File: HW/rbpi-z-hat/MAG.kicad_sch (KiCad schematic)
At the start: 0 parts

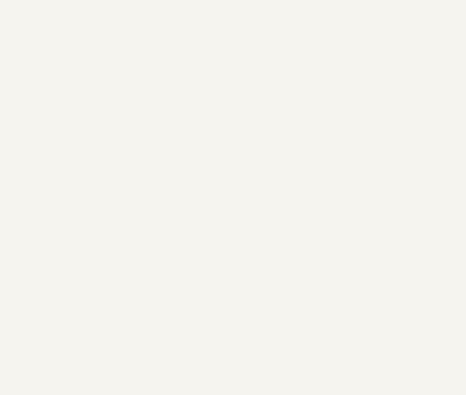
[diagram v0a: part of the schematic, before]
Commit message: Added schematics for QMC5883L
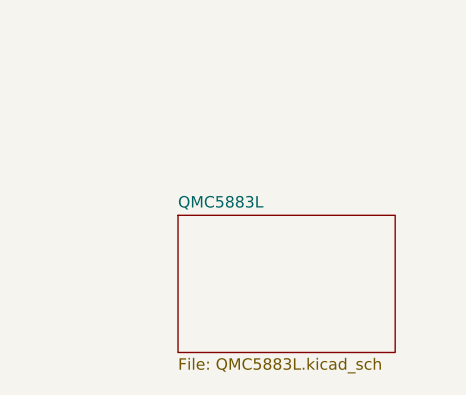
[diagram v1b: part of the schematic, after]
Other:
- added sheet QMC5883L (QMC5883L.kicad_sch)
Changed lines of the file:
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@@
     (stroke (width 0) (type default))
+  )
+  (sheet (at 85.09 142.24) (size 24.13 15.24) (fields_autoplaced)
+    (stroke (width 0.1524) (type solid))
+    (fill (color 0 0 0 0.0000))
+    (property "Sheetname" "QMC5883L" (at 85.09 141.5284 0)
+      (effects (font (size 1.27 1.27)) (justify left bottom))
+    )
+    (property "Sheetfile" "QMC5883L.kicad_sch" (at 85.09 158.0646 0)
+      (effects (font (size 1.27 1.27)) (justify left top))
+    )
+    (instances
+      (project "rbpi-z-hat"
+        (path "/d99b0340-d795-4b40-9cde-9851c6cee99d/740a9ed9-3c23-4e4f-8dd1-04f07ce4215e" (page "19"))
+      )
+    )
   )
   (sheet (at 82.55 74.93) (size 24.13 21.59) (fields_autoplaced)

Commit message: Apdated Sch and PCB
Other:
- sheet QMC5883L ports: added QMC_GND, QMC_INT, QMC_SCL, QMC_SDA, QMC_VDD; removed none
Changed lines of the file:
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@@
     (comment 2 "Denis Tsekh")
   )
-  (wire (pts (xy 67.31 93.98) (xy 82.55 93.98))
+  (junction (at 95.25 139.7) (diameter 0) (color 0 0 0 0)
+  )
+  (junction (at 104.14 128.27) (diameter 0) (color 0 0 0 0)
+  )
+  (junction (at 97.79 142.24) (diameter 0) (color 0 0 0 0)
+  )
+  (junction (at 101.6 125.73) (diameter 0) (color 0 0 0 0)
+  )
+  (wire (pts (xy 91.44 142.24) (xy 97.79 142.24))
     (stroke (width 0) (type default))
   )
-  (wire (pts (xy 67.31 77.47) (xy 82.55 77.47))
+  (wire (pts (xy 91.44 125.73) (xy 101.6 125.73))
     (stroke (width 0) (type default))
   )
-  (wire (pts (xy 67.31 83.82) (xy 82.55 83.82))
+  (wire (pts (xy 104.14 128.27) (xy 106.68 128.27))
     (stroke (width 0) (type default))
   )
-  (wire (pts (xy 67.31 80.01) (xy 82.55 80.01))
+  (wire (pts (xy 91.44 132.08) (xy 106.68 132.08))
     (stroke (width 0) (type default))
   )
-  (wire (pts (xy 67.31 86.36) (xy 82.55 86.36))
+  (wire (pts (xy 104.14 128.27) (xy 104.14 161.29))
     (stroke (width 0) (type default))
   )
-  (wire (pts (xy 67.31 91.44) (xy 82.55 91.44))
+  (wire (pts (xy 91.44 128.27) (xy 104.14 128.27))
     (stroke (width 0) (type default))
   )
-  (sheet (at 85.09 142.24) (size 24.13 15.24) (fields_autoplaced)
+  (wire (pts (xy 104.14 161.29) (xy 106.68 161.29))
+    (stroke (width 0) (type default))
+  )
+  (wire (pts (xy 95.25 139.7) (xy 95.25 167.64))
+    (stroke (width 0) (type default))
+  )
+  (wire (pts (xy 97.79 170.18) (xy 106.68 170.18))
+    (stroke (width 0) (type default))
+  )
+  (wire (pts (xy 101.6 158.75) (xy 106.68 158.75))
+    (stroke (width 0) (type default))
+  )
+  (wire (pts (xy 95.25 139.7) (xy 106.68 139.7))
+    (stroke (width 0) (type default))
+  )
+  (wire (pts (xy 91.44 134.62) (xy 106.68 134.62))
+    (stroke (width 0) (type default))
+  )
+  (wire (pts (xy 91.44 163.83) (xy 106.68 163.83))
+    (stroke (width 0) (type default))
+  )
+  (wire (pts (xy 97.79 142.24) (xy 106.68 142.24))
+    (stroke (width 0) (type default))
+  )
+  (wire (pts (xy 95.25 167.64) (xy 106.68 167.64))
+    (stroke (width 0) (type default))
+  )
+  (wire (pts (xy 91.44 139.7) (xy 95.25 139.7))
+    (stroke (width 0) (type default))
+  )
+  (wire (pts (xy 101.6 125.73) (xy 101.6 158.75))
+    (stroke (width 0) (type default))
+  )
+  (wire (pts (xy 97.79 142.24) (xy 97.79 170.18))
+    (stroke (width 0) (type default))
+  )
+  (wire (pts (xy 101.6 125.73) (xy 106.68 125.73))
+    (stroke (width 0) (type default))
+  )
+  (hierarchical_label "MAG_SDA" (shape bidirectional) (at 91.44 125.73 180) (fields_autoplaced)
+    (effects (font (size 1.27 1.27)) (justify right))
+  )
+  (hierarchical_label "MAG_SCL" (shape input) (at 91.44 128.27 180) (fields_autoplaced)
+    (effects (font (size 1.27 1.27)) (justify right))
+  )
+  (hierarchical_label "MAG_GND" (shape input) (at 91.44 142.24 180) (fields_autoplaced)
+    (effects (font (size 1.27 1.27)) (justify right))
+  )
+  (hierarchical_label "MAG_IST_nRST" (shape input) (at 91.44 132.08 180) (fields_autoplaced)
+    (effects (font (size 1.27 1.27)) (justify right))
+  )
+  (hierarchical_label "MAG_VDD" (shape input) (at 91.44 139.7 180) (fields_autoplaced)
+    (effects (font (size 1.27 1.27)) (justify right))
+  )
+  (hierarchical_label "MAG_QMC_INT" (shape output) (at 91.44 163.83 180) (fields_autoplaced)
+    (effects (font (size 1.27 1.27)) (justify right))
+  )
+  (hierarchical_label "MAG_IST_DRDY" (shape output) (at 91.44 134.62 180) (fields_autoplaced)
+    (effects (font (size 1.27 1.27)) (justify right))
+  )
+  (sheet (at 106.68 156.21) (size 26.67 16.51) (fields_autoplaced)
     (stroke (width 0.1524) (type solid))
     (fill (color 0 0 0 0.0000))
-    (property "Sheetname" "QMC5883L" (at 85.09 141.5284 0)
+    (property "Sheetname" "QMC5883L" (at 106.68 155.4984 0)
       (effects (font (size 1.27 1.27)) (justify left bottom))
     )
-    (property "Sheetfile" "QMC5883L.kicad_sch" (at 85.09 158.0646 0)
+    (property "Sheetfile" "QMC5883L.kicad_sch" (at 106.68 173.3046 0)
       (effects (font (size 1.27 1.27)) (justify left top))
+    )
+    (pin "QMC_VDD" input (at 106.68 167.64 180)
+      (effects (font (size 1.27 1.27)) (justify left))
+    )
+    (pin "QMC_SCL" input (at 106.68 161.29 180)
+      (effects (font (size 1.27 1.27)) (justify left))
+    )
+    (pin "QMC_SDA" bidirectional (at 106.68 158.75 180)
+      (effects (font (size 1.27 1.27)) (justify left))
+    )
+    (pin "QMC_GND" input (at 106.68 170.18 180)
+      (effects (font (size 1.27 1.27)) (justify left))
+    )
+    (pin "QMC_INT" output (at 106.68 163.83 180)
+      (effects (font (size 1.27 1.27)) (justify left))
     )
     (instances
@@
     )
   )
-  (sheet (at 82.55 74.93) (size 24.13 21.59) (fields_autoplaced)
+  (sheet (at 106.68 123.19) (size 24.13 21.59) (fields_autoplaced)
     (stroke (width 0.1524) (type solid))
     (fill (color 0 0 0 0.0000))
-    (property "Sheetname" "IST8310" (at 82.55 74.2184 0)
+    (property "Sheetname" "IST8310" (at 106.68 122.4784 0)
       (effects (font (size 1.27 1.27)) (justify left bottom))
     )
-    (property "Sheetfile" "IST8310.kicad_sch" (at 82.55 97.1046 0)
+    (property "Sheetfile" "IST8310.kicad_sch" (at 106.68 145.3646 0)
       (effects (font (size 1.27 1.27)) (justify left top))
     )
-    (pin "IST_GND" input (at 82.55 93.98 180)
+    (pin "IST_GND" input (at 106.68 142.24 180)
       (effects (font (size 1.27 1.27)) (justify left))
     )
-    (pin "IST_VDD" input (at 82.55 91.44 180)
+    (pin "IST_VDD" input (at 106.68 139.7 180)
       (effects (font (size 1.27 1.27)) (justify left))
     )
-    (pin "IST_SDA" bidirectional (at 82.55 77.47 180)
+    (pin "IST_SDA" bidirectional (at 106.68 125.73 180)
       (effects (font (size 1.27 1.27)) (justify left))
     )
-    (pin "IST_SCL" input (at 82.55 80.01 180)
+    (pin "IST_SCL" input (at 106.68 128.27 180)
       (effects (font (size 1.27 1.27)) (justify left))
     )
-    (pin "IST_nRST" input (at 82.55 83.82 180)
+    (pin "IST_nRST" input (at 106.68 132.08 180)
       (effects (font (size 1.27 1.27)) (justify left))
     )
-    (pin "IST_DRDY" output (at 82.55 86.36 180)
+    (pin "IST_DRDY" output (at 106.68 134.62 180)
       (effects (font (size 1.27 1.27)) (justify left))
     )
